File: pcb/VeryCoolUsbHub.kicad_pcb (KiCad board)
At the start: 4 copper layers, 80.7 x 55.9 mm, 67 parts, among them U1 HD3SS3220RNHR, U2 HD3SS3220RNHR, X1 X322525MSB4SI, X2 X322525MSB4SI

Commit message: screwhole
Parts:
- added REF**: MountingHole_2.2mm_M2_DIN965_Pad, MountingHole:MountingHole_2.2mm_M2_DIN965_Pad, F.Cu at (241.2, 33.0)
- added REF**: MountingHole_2.2mm_M2_DIN965_Pad, MountingHole:MountingHole_2.2mm_M2_DIN965_Pad, F.Cu at (169.8, 82.1)
- moved G*** 2.31 mm to (214.4, 57.2)
- moved G*** 1.93 mm to (233.8, 37.0)
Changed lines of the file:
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@@
 	(footprint "LOGO"
 		(layer "F.Cu")
-		(at 233.1 35.2)
+		(at 233.8 37)
 		(property "Reference" "G***"
 			(at 0 0 0)
@@
 		)
 	)
+	(footprint "MountingHole:MountingHole_2.2mm_M2_DIN965_Pad"
+		(layer "F.Cu")
+		(at 241.2 33)
+		(descr "Mounting Hole 2.2mm, M2, generated by kicad-footprint-generator mountinghole.py")
+		(tags "mountinghole M2 DIN965")
+		(property "Reference" "REF**"
+			(at 0 -2.85 0)
+			(layer "F.SilkS")
+			(hide yes)
+			(effects
+				(font
+					(size 1 1)
+					(thickness 0.15)
+				)
+			)
+		)
+		(property "Value" "MountingHole_2.2mm_M2_DIN965_Pad"
+			(at 0 2.85 0)
+			(layer "F.Fab")
+			(effects
+				(font
+					(size 1 1)
+					(thickness 0.15)
+				)
+			)
+		)
+		(property "Datasheet" ""
+			(at 0 0 0)
+			(layer "F.Fab")
+			(hide yes)
+			(effects
+				(font
+					(size 1.27 1.27)
+					(thickness 0.15)
+				)
+			)
+		)
+		(property "Description" ""
+			(at 0 0 0)
+			(layer "F.Fab")
+			(hide yes)
+			(effects
+				(font
+					(size 1.27 1.27)
+					(thickness 0.15)
+				)
+			)
+		)
+		(attr exclude_from_pos_files exclude_from_bom)
+		(fp_circle
+			(center 0 0)
+			(end 1.9 0)
+			(stroke
+				(width 0.15)
+				(type solid)
+			)
+			(fill no)
+			(layer "Cmts.User")
+		)
+		(fp_circle
+			(center 0 0)
+			(end 2.15 0)
+			(stroke
+				(width 0.05)
+				(type solid)
+			)
+			(fill no)
+			(layer "F.CrtYd")
+		)
+		(fp_text user "${REFERENCE}"
+			(at 0 0 0)
+			(layer "F.Fab")
+			(effects
+				(font
+					(size 0.95 0.95)
+					(thickness 0.14)
+				)
+			)
+		)
+		(pad "1" thru_hole circle
+			(at 0 0)
+			(size 3.8 3.8)
+			(drill 2.2)
+			(layers "*.Cu" "*.Mask")
+			(remove_unused_layers no)
+			(zone_connect 2)
+		)
+		(embedded_fonts no)
+	)
 	(footprint "Resistor_SMD:R_0402_1005Metric"
 		(layer "F.Cu")
@@
 		)
 	)
+	(footprint "MountingHole:MountingHole_2.2mm_M2_DIN965_Pad"
+		(layer "F.Cu")
+		(at 169.8 82.1)
+		(descr "Mounting Hole 2.2mm, M2, generated by kicad-footprint-generator mountinghole.py")
+		(tags "mountinghole M2 DIN965")
+		(property "Reference" "REF**"
+			(at 0 -2.85 0)
+			(layer "F.SilkS")
+			(hide yes)
+			(effects
+				(font
+					(size 1 1)
+					(thickness 0.15)
+				)
+			)
+		)
+		(property "Value" "MountingHole_2.2mm_M2_DIN965_Pad"
+			(at 0 2.85 0)
+			(layer "F.Fab")
+			(effects
+				(font
+					(size 1 1)
+					(thickness 0.15)
+				)
+			)
+		)
+		(property "Datasheet" ""
+			(at 0 0 0)
+			(layer "F.Fab")
+			(hide yes)
+			(effects
+				(font
+					(size 1.27 1.27)
+					(thickness 0.15)
+				)
+			)
+		)
+		(property "Description" ""
+			(at 0 0 0)
+			(layer "F.Fab")
+			(hide yes)
+			(effects
+				(font
+					(size 1.27 1.27)
+					(thickness 0.15)
+				)
+			)
+		)
+		(attr exclude_from_pos_files exclude_from_bom)
+		(fp_circle
+			(center 0 0)
+			(end 1.9 0)
+			(stroke
+				(width 0.15)
+				(type solid)
+			)
+			(fill no)
+			(layer "Cmts.User")
+		)
+		(fp_circle
+			(center 0 0)
+			(end 2.15 0)
+			(stroke
+				(width 0.05)
+				(type solid)
+			)
+			(fill no)
+			(layer "F.CrtYd")
+		)
+		(fp_text user "${REFERENCE}"
+			(at 0 0 0)
+			(layer "F.Fab")
+			(effects
+				(font
+					(size 0.95 0.95)
+					(thickness 0.14)
+				)
+			)
+		)
+		(pad "1" thru_hole circle
+			(at 0 0)
+			(size 3.8 3.8)
+			(drill 2.2)
+			(layers "*.Cu" "*.Mask")
+			(remove_unused_layers no)
+			(zone_connect 2)
+		)
+		(embedded_fonts no)
+	)
 	(footprint "EasyEDA:USB-3.0-A-TH_HC-ST-003-01-Z"
 		(layer "F.Cu")
@@
 	(footprint "LOGO"
 		(layer "B.Cu")
-		(at 212.1 57 180)
+		(at 214.4 57.2 180)
 		(property "Reference" "G***"
 			(at 0 0 0)
@@
 	)
 	(gr_text "Ethernet Controler\n"
-		(at 219.8 42.8 0)
+		(at 220.6 44.4 0)
 		(layer "F.SilkS")
 		(effects
@@
 	)
 	(gr_text "made with love from duykhanh09103 <3\nme@duykhanh09103.dev\n"
-		(at 181.3 84.1 0)
+		(at 189.3 84.2 0)
 		(layer "B.SilkS")
 		(effects

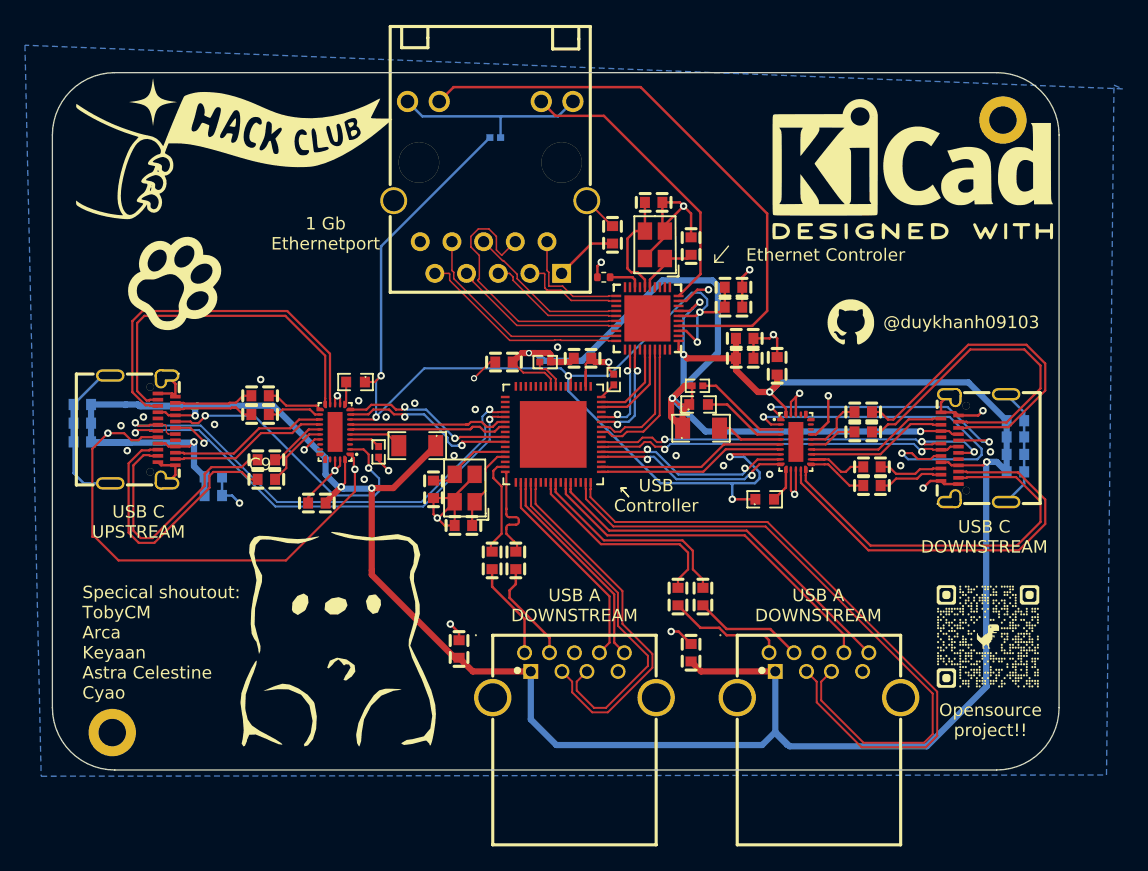
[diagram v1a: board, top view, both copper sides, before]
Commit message: fix connector and add case
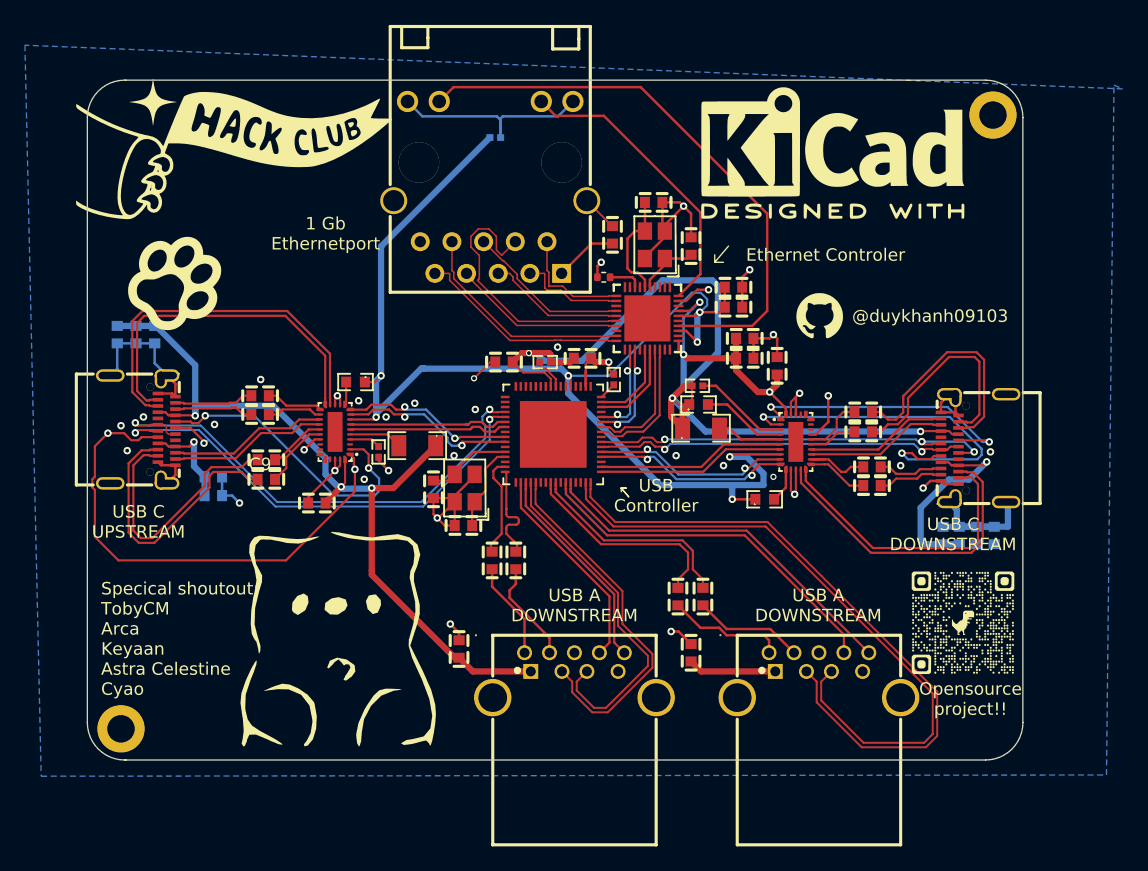
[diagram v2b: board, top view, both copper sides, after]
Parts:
- moved C4 10.9 mm to (236.4, 66.3), turned to 90 degrees
- moved C30 10.4 mm to (173.2, 50.2), turned to -90 degrees
- moved C3 9.09 mm to (237.7, 66.3), turned to 90 degrees
- moved C31 8.30 mm to (171.7, 50.2), turned to 90 degrees
- moved C2 7.20 mm to (239.1, 66.3), turned to 90 degrees
- moved G*** 6.53 mm to (227.4, 35.7)
- moved C32 6.26 mm to (170.2, 50.2), turned to -90 degrees
- moved C1 5.38 mm to (240.5, 66.3), turned to 90 degrees
- moved G*** 2.55 mm to (226.5, 48.7)
- moved G*** 2.28 mm to (238.0, 73.3)
- moved G*** 1.73 mm to (172.7, 37.4)
- moved REF** 0.89 mm to (240.4, 32.6)
- moved REF** 0.76 mm to (170.5, 81.8)
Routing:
- net VBUS: track 330.3 -> 201.0 mm
- net /V3.3: track 104.0 -> 126.8 mm
- net /USBC_OUT_RXP1: track 31.7 -> 23.5 mm
- net /USBC_OUT_RXN1: track 33.6 -> 25.4 mm
- net /USBC_OUT_TXP2: track 26.3 -> 18.2 mm
- net /USBC_OUT_TXN2: track 27.6 -> 19.5 mm
- net Net-(R6-Pad1): track 16.0 -> 17.4 mm
- net GND: track 114.8 -> 113.6 mm, vias 37 -> 36
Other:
- board size 80.7 x 55.9 mm -> 75 x 54.5 mm

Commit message: forgor to update
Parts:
- moved C36 3.99 mm to (220.8, 69.6)
- moved C37 3.99 mm to (218.8, 69.6)
- moved C20 1.02 mm to (181.3, 62.4)
- moved C21 1.02 mm to (181.3, 60.8)
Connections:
- net Net-(U1-TX1n) renamed C_TXP1
- net Net-(U1-TX1p) renamed C_TXN1
- net Net-(U1-TX2n) renamed C_TXP2
- net Net-(U1-TX2p) renamed C_TXN2
- net Net-(U2-TX1n) renamed IN_C_TXP1
- net Net-(U2-TX1p) renamed IN_C_TXN1
- net Net-(U2-TX2n) renamed IN_C_TXP2
- net Net-(U2-TX2p) renamed IN_C_TXN2
- net Net-(USB_OUT_1-StdA_SSTX+) renamed USB_TXN1
- net Net-(USB_OUT_1-StdA_SSTX-) renamed USB_TXP1
- net Net-(USB_OUT_2-StdA_SSTX+) renamed TXN2+
- net Net-(USB_OUT_2-StdA_SSTX-) renamed TXN2-
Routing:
- net /MDIN1: track 13.8 -> 21.9 mm
- net GND: track 113.6 -> 116.6 mm, vias 36 -> 35
- net IN_C_TXP2: track 4.62 -> 7.20 mm
- net /DP0: track 41.5 -> 44.0 mm
- net /TXN2: track 17.0 -> 19.3 mm
- net /DP3: track 29.7 -> 31.9 mm
- net /TXP2: track 17.0 -> 19.3 mm
- net /MDIP2: track 11.0 -> 13.1 mm
- net /USBC_OUT_RXP1: track 23.5 -> 25.3 mm
- net /USBC_IN_RXP1: track 28.0 -> 29.8 mm
- net IN_C_TXN2: track 5.61 -> 7.20 mm
- net /USBC_IN_TXN2: track 22.2 -> 21.0 mm
- net /USBC_OUT_TXP2: track 18.2 -> 19.4 mm
- net /DP2: track 52.1 -> 53.3 mm
- net /DP1: track 28.1 -> 29.3 mm
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
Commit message: fixed some signal intergrity problem
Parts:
- moved C36 2.01 mm to (219.9, 71.4)
- moved C37 2.01 mm to (217.9, 71.4)
- moved C12 0.09 mm to (209.8, 42.1)
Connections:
- U1 pad 31: unconnected-(U1-EP-Pad31) -> GND
- U2 pad 31: unconnected-(U2-EP-Pad31) -> GND
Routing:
- net GND: track 116.6 -> 122.1 mm, vias 35 -> 30
- net /DN2: track 53.3 -> 55.2 mm
- net /DP2: track 53.3 -> 55.1 mm
- net /MDIP1: track 22.1 -> 21.3 mm
- net /MDIN1: track 21.9 -> 21.1 mm
- net TXN2-: track 9.92 -> 9.34 mm
